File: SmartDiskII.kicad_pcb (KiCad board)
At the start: 2 copper layers, 100 x 77.5 mm, 32 parts, among them J1 DRIVE 2, J2 DRIVE 1, J3 Apple II Expansion Slot, U1 74LS174, U10 74LS245, U11 74LS323, U12 74LS00, U13 74LS20, U2 NE556, U3 74LS05, U4 74LS132, U5 74LS259/9334, U6 74LS21, U7 2758/16/32 P6, U8 74LS30, U9 2732

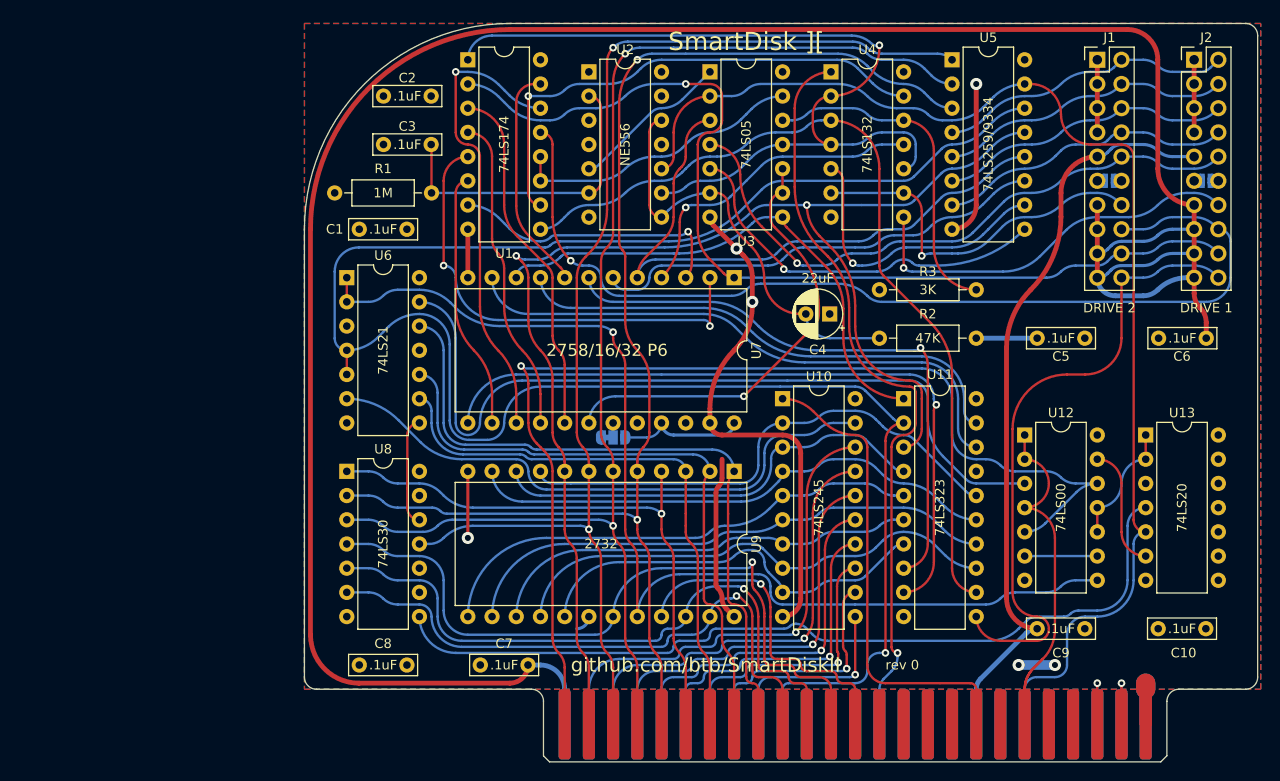
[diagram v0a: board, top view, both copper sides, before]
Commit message: new revision
only one drive connector, configurable with jumpers
optionally use 2764 EPROM
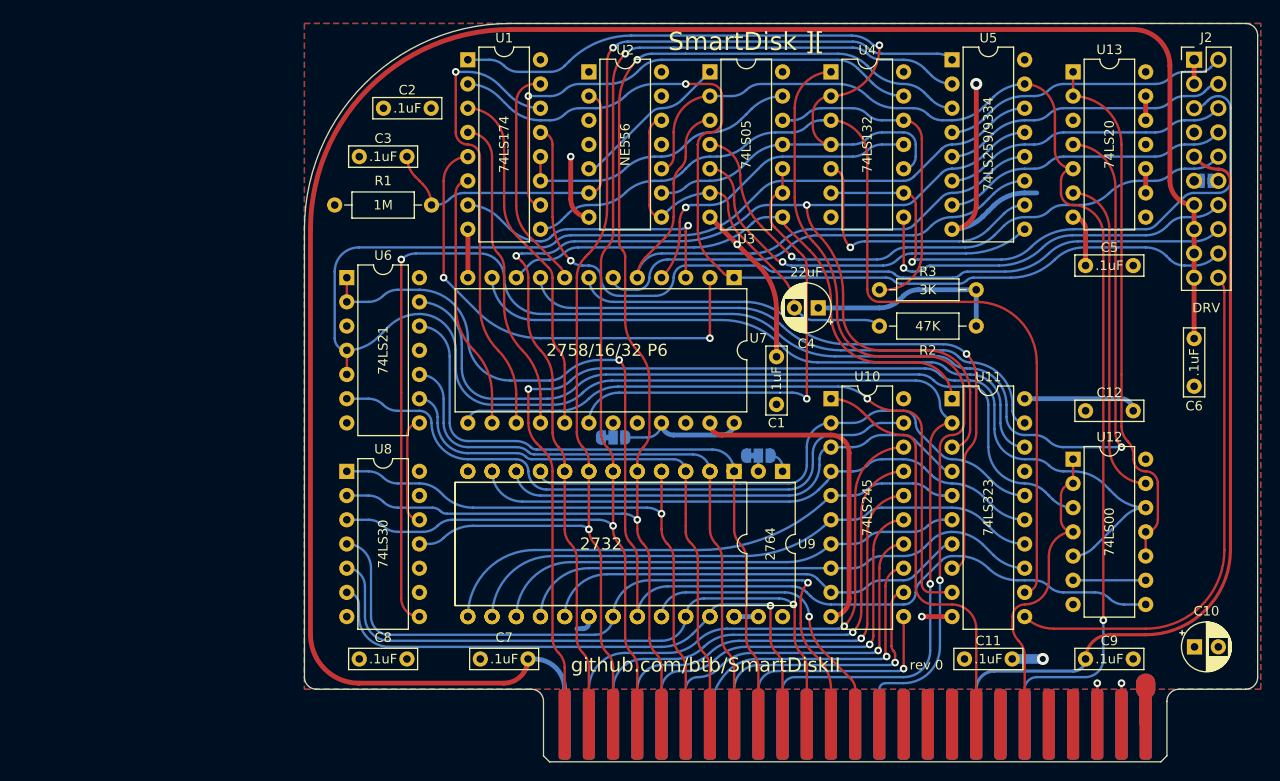
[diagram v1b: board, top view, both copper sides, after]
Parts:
- removed the J1 at (194.3, 67.3)
- removed JP2: 5V on Disk 2 Pin 12, Jumper:SolderJumper-2_P1.3mm_Open_RoundedPad1.0x1.5mm
- added ALTU9: 2764, Package_DIP:DIP-28_W15.24mm, F.Cu at (161.3, 110.5)
- added C11: .1uF, Capacitor_THT:C_Rect_L7.0mm_W2.0mm_P5.00mm, F.Cu at (185.4, 130.2)
- added C12: .1uF, Capacitor_THT:C_Rect_L7.0mm_W2.0mm_P5.00mm, F.Cu at (198.1, 104.1)
- added JP4: A12H/L, Jumper:SolderJumper-3_P1.3mm_Bridged12_RoundedPad1.0x1.5mm_NumberLabels, B.Cu at (158.8, 108.8)
- C10: value .1uF -> 22uF; footprint Capacitor_THT:C_Rect_L7.0mm_W2.0mm_P5.00mm -> Capacitor_THT:CP_Radial_D5.0mm_P2.50mm
- J2: value DRIVE 1 -> DRV
- moved C1 47.5 mm to (160.7, 103.5), turned to 90 degrees
- moved U13 38.9 mm to (191.8, 68.6)
- moved C5 12.6 mm to (198.1, 88.9), turned to 180 degrees
- moved R3 10.2 mm to (181.6, 91.4), turned to 180 degrees
- moved C9 5.99 mm to (193.1, 130.2)
- moved U12 5.68 mm to (191.8, 109.2)
- moved U10 5.08 mm to (166.4, 102.9)
- moved U11 5.08 mm to (179.1, 102.9)
- moved C10 4.26 mm to (204.5, 128.9)
- moved C3 2.84 mm to (121.9, 77.5)
- moved C4 1.36 mm to (165.0, 93.3)
- moved C6 1.27 mm to (204.5, 96.6), turned to -90 degrees
- moved C2 1.27 mm to (124.4, 72.4)
- moved R1 1.27 mm to (114.3, 82.5)
- moved R2 1.27 mm to (171.4, 95.2)
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- renumbered J3 to J1
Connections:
- net /SEL1 renamed /SEL
- J2 pad 5: GND -> /~{ENBL 2}
- J2 pad 7: GND -> unconnected-(J2-Pin_7-Pad7)
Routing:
- net /~{HISTROBE}: track 89.6 -> 157.9 mm, vias 0 -> 2
- net /ENCOMMON: track 12.9 -> 55.8 mm
- net +12V: track 252.2 -> 211.9 mm
- net /~{ENBL 2}: track 38.6 -> 64.5 mm
- net /CLRCOMMON: track 12.9 -> 34.5 mm
- net /RD DATA: track 104.4 -> 87.7 mm
- net +5V: track 45.4 -> 58.9 mm, vias 2 -> 1
- net /W PROT: track 66.3 -> 54.4 mm
- net Net-(U1-Cp): track 89.9 -> 100.0 mm
- net GND: track 103.9 -> 113.9 mm
- net /Q3: track 78.0 -> 86.7 mm
- net /~{ENROM}: track 115.7 -> 123.7 mm
- net /~{IOSTROBE}: track 39.5 -> 32.9 mm
- net /~{ENBUF}: track 60.9 -> 67.1 mm
- net /R/W: track 50.0 -> 44.1 mm
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
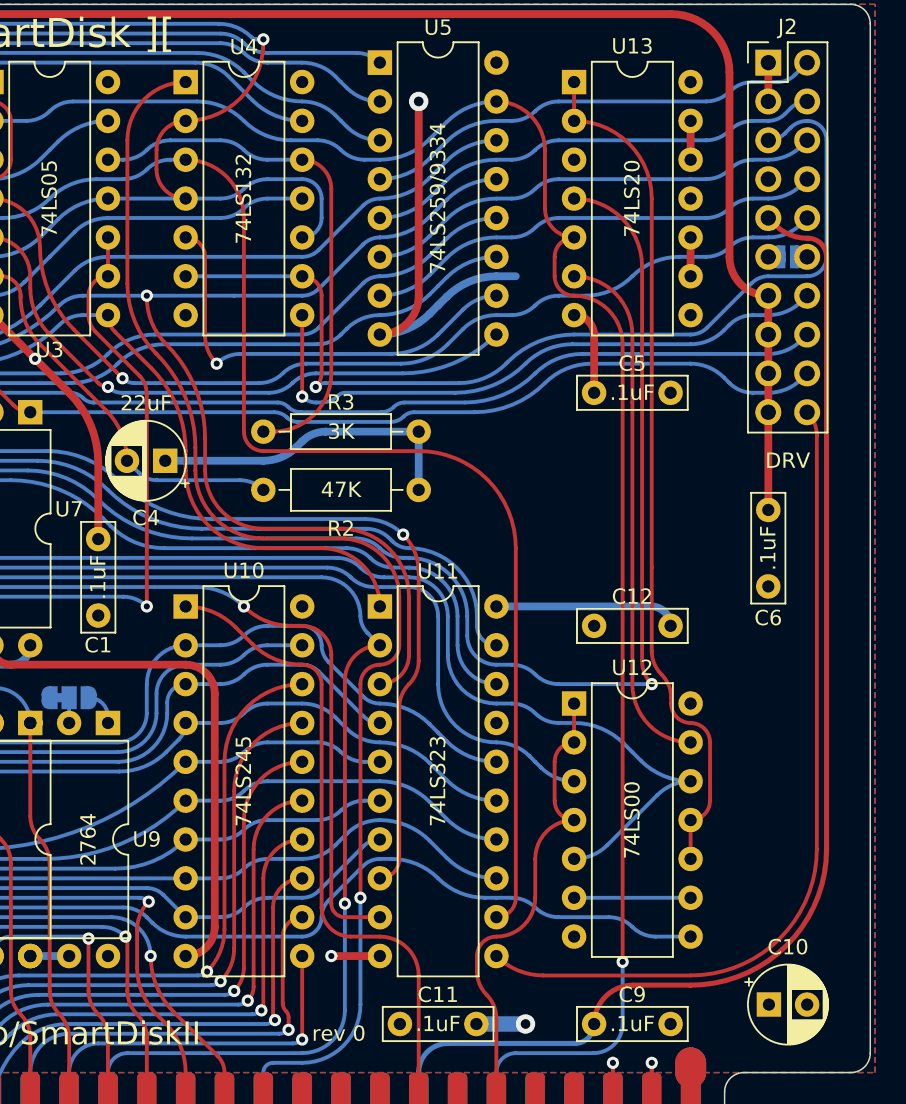
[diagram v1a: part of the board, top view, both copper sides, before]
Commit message: use liron pinout with jumpers for EN2
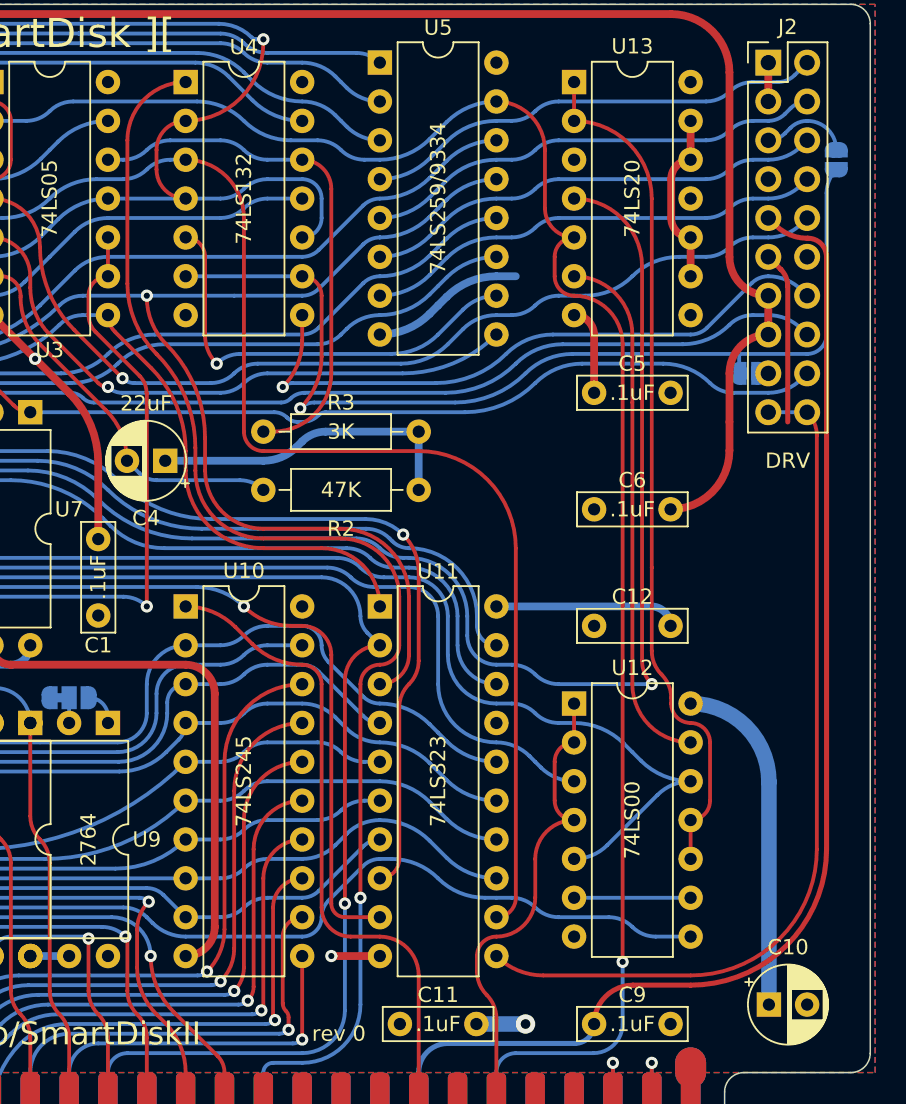
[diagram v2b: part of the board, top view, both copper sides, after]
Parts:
- added JP2: ~, Jumper:SolderJumper-2_P1.3mm_Open_RoundedPad1.0x1.5mm, B.Cu at (208.9, 73.7)
- JP1: value 5V on Disk 1 Pin 12 -> ~
- moved JP1 8.03 mm to (203.2, 87.6)
- moved C6 6.39 mm to (198.1, 96.5), turned to 180 degrees
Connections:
- J2 pad 17: +12V -> Net-(J2-Pin_17)
- J2 pad 19: +12V -> /W PROT
- J2 pad 5: /~{ENBL 2} -> Net-(J2-Pin_5)
- JP1 pad 1: +5V -> /~{ENBL 2}
- JP1 pad 2: /SEL -> Net-(J2-Pin_17)
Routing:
- net +5V: track 58.9 -> 92.6 mm
- net GND: track 113.9 -> 103.7 mm, vias 4 -> 3
- net Net-(J2-Pin_5): track 0.00 -> 5.83 mm
- net +12V: track 211.9 -> 215.3 mm
- net /W PROT: track 54.4 -> 56.9 mm
- net /~{ENBL 1}: track 40.3 -> 42.0 mm
- net /~{ENBL 2}: track 64.5 -> 65.5 mm

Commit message: update kicad files
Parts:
- added JP10: SolderJumper_2_Bridged, Jumper:SolderJumper-2_P1.3mm_Bridged_RoundedPad1.0x1.5mm, B.Cu at (112.4, 109.2)
- added JP11: SolderJumper_2_Bridged, Jumper:SolderJumper-2_P1.3mm_Bridged_RoundedPad1.0x1.5mm, B.Cu at (112.4, 101.6)
- added JP5: A13H/L, Connector_PinHeader_2.54mm:PinHeader_1x03_P2.54mm_Horizontal, F.Cu at (112.4, 118.1)
- added JP6: A14H/L, Connector_PinHeader_2.54mm:PinHeader_1x03_P2.54mm_Horizontal, F.Cu at (112.4, 110.5)
- added JP7: A15H/L, Connector_PinHeader_2.54mm:PinHeader_1x03_P2.54mm_Horizontal, F.Cu at (112.4, 102.9)
- added JP8: SolderJumper_2_Bridged, Jumper:SolderJumper-2_P1.3mm_Bridged_RoundedPad1.0x1.5mm, B.Cu at (112.4, 124.5)
- added JP9: SolderJumper_2_Bridged, Jumper:SolderJumper-2_P1.3mm_Bridged_RoundedPad1.0x1.5mm, B.Cu at (112.4, 116.8)
- added R4: 3K, Resistor_THT:R_Axial_DIN0207_L6.3mm_D2.5mm_P10.16mm_Horizontal, F.Cu at (198.1, 100.3)
- J2: footprint Connector_PinHeader_2.54mm:PinHeader_2x10_P2.54mm_Vertical -> MyConnector:PinHeader_2x10_P2.54mm_Vertical_Shrouded
- JP4: footprint Jumper:SolderJumper-3_P1.3mm_Bridged12_RoundedPad1.0x1.5mm_NumberLabels -> Connector_PinHeader_2.54mm:PinHeader_1x03_P2.54mm_Horizontal; moved to F.Cu
- moved JP4 49.3 mm to (112.4, 125.7), turned to 180 degrees
- moved JP3 3.43 mm to (143.5, 103.5), turned to 180 degrees
- moved C3 2.54 mm to (124.4, 77.5)
- moved J2 1.42 mm to (205.1, 68.6)
- moved JP2 0.90 mm to (209.6, 73.0)
- moved JP1 0.64 mm to (203.2, 88.3), turned to -90 degrees
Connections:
- net Net-(ALTU9-A12) renamed /FWA12
- ALTU9 pad 1: +5V -> /FWA15
- ALTU9 pad 26: +5V -> /FWA13
- ALTU9 pad 27: +5V -> /FWA14
- JP4 pad 1: GND -> +5V
- JP4 pad 3: +5V -> GND
- U9 pad 24: +5V -> /FWA13
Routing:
- net GND: track 103.7 -> 173.7 mm
- net /FWA15: track 0.00 -> 63.2 mm
- net /FWA12: track 1.65 -> 60.2 mm, vias 0 -> 1
- net /FWA14: track 0.00 -> 58.2 mm, vias 0 -> 1
- net /FWA13: track 0.00 -> 52.8 mm, vias 0 -> 1
- net Net-(U7-~{CE}): track 50.9 -> 78.2 mm, vias 1 -> 2
- net +5V: track 92.6 -> 114.6 mm
- net /~{IOSEL}: track 118.3 -> 126.3 mm
- net /IOSTROBE: track 84.4 -> 77.8 mm
- net /A4: track 61.4 -> 64.4 mm
- net Net-(J2-Pin_17): track 0.00 -> 1.91 mm
- net Net-(U11-SR): track 70.5 -> 72.3 mm
- net /R4: track 61.7 -> 59.9 mm
- net /R3: track 56.6 -> 54.8 mm
- net /R5: track 49.9 -> 48.3 mm
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
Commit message: rev2
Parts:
- removed JP10, JP11, JP8, JP9: SolderJumper_2_Bridged, Jumper:SolderJumper-2_P1.3mm_Bridged_RoundedPad1.0x1.5mm
- removed the JP4 at (112.4, 125.7)
- added C13: 100n, Capacitor_THT:C_Disc_D4.3mm_W1.9mm_P5.00mm, F.Cu at (193.0, 130.2)
- added C14: 100n, Capacitor_THT:C_Disc_D4.3mm_W1.9mm_P5.00mm, F.Cu at (205.7, 125.7)
- added JP3: ~, Jumper:SolderJumper-2_P1.3mm_Open_RoundedPad1.0x1.5mm, B.Cu at (206.4, 91.4)
- added R5: 10K, Resistor_THT:R_Axial_DIN0207_L6.3mm_D2.5mm_P10.16mm_Horizontal, F.Cu at (114.9, 90.2)
- added R6: 10K, Resistor_THT:R_Axial_DIN0207_L6.3mm_D2.5mm_P10.16mm_Horizontal, F.Cu at (114.9, 102.9)
- added R7: 10K, Resistor_THT:R_Axial_DIN0207_L6.3mm_D2.5mm_P10.16mm_Horizontal, F.Cu at (118.7, 102.9)
- added R8: 10K, Resistor_THT:R_Axial_DIN0207_L6.3mm_D2.5mm_P10.16mm_Horizontal, F.Cu at (118.7, 90.2)
- added SJP10: ~, Jumper:SolderJumper-2_P1.3mm_Bridged_RoundedPad1.0x1.5mm, F.Cu at (117.5, 118.1)
- added SJP8: ~, Jumper:SolderJumper-2_P1.3mm_Bridged_RoundedPad1.0x1.5mm, F.Cu at (117.5, 123.2)
- added SJP9: ~, Jumper:SolderJumper-2_P1.3mm_Bridged_RoundedPad1.0x1.5mm, F.Cu at (117.5, 120.7)
- ALTU10: renamed from ALTU9; value 2764 -> '64-'512
- C1: renamed from C4; value 22uF -> 22u
- C10: renamed from C2; value .1uF -> 100n; footprint Capacitor_THT:C_Rect_L7.0mm_W2.0mm_P5.00mm -> Capacitor_THT:C_Disc_D4.3mm_W1.9mm_P5.00mm
- C11, C12, C3, C5, C6, C7, C8, C9: value .1uF -> 100n; footprint Capacitor_THT:C_Rect_L7.0mm_W2.0mm_P5.00mm -> Capacitor_THT:C_Disc_D4.3mm_W1.9mm_P5.00mm
- C2: renamed from C10; value 22uF -> 22u
- C4: renamed from C1; value .1uF -> 100n; footprint Capacitor_THT:C_Rect_L7.0mm_W2.0mm_P5.00mm -> Capacitor_THT:C_Disc_D4.3mm_W1.9mm_P5.00mm
- JP5: value A13H/L -> ~; footprint Connector_PinHeader_2.54mm:PinHeader_1x03_P2.54mm_Horizontal -> Connector_PinHeader_2.54mm:PinHeader_1x02_P2.54mm_Vertical
- JP6: value A14H/L -> ~; footprint Connector_PinHeader_2.54mm:PinHeader_1x03_P2.54mm_Horizontal -> Connector_PinHeader_2.54mm:PinHeader_1x02_P2.54mm_Vertical
- JP7: value A15H/L -> ~; footprint Connector_PinHeader_2.54mm:PinHeader_1x03_P2.54mm_Horizontal -> Connector_PinHeader_2.54mm:PinHeader_1x02_P2.54mm_Vertical
- moved C8 91.9 mm to (198.7, 88.3), turned to 180 degrees
- moved C10 81.2 mm to (200.7, 100.3), turned to 0 degrees
- moved C12 73.8 mm to (129.5, 131.4)
- moved C11 70.4 mm to (115.0, 128.9), turned to 0 degrees
- moved C5 49.3 mm to (151.1, 73.7), turned to -90 degrees
- moved C4 46.9 mm to (117.5, 85.1), turned to 0 degrees
- moved C7 42.5 mm to (167.6, 103.5), turned to 90 degrees
- moved C9 38.7 mm to (193.7, 91.4)
- moved C6 31.0 mm to (177.2, 73.7), turned to -90 degrees
- moved JP7 16.5 mm to (118.8, 118.1), turned to -90 degrees
- moved JP6 12.0 mm to (118.8, 120.7), turned to -90 degrees
- moved U13 8.52 mm to (199.4, 105.4)
- moved JP5 8.14 mm to (118.8, 123.2), turned to -90 degrees
- moved ALTU10 7.62 mm to (168.9, 110.5)
- moved JP4 7.62 mm to (151.1, 103.5), turned to 0 degrees
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- renumbered JP2 to JP1, JP1 to JP2, JP3 to JP4, U9 to U10, U10 to U11, U11 to U12, U12 to U13, U13 to U6, U6 to U7, U7 to U8, U8 to U9
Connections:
- ALTU10 pad 1: /FWA15 -> Net-(ALTU10-A14)
- ALTU10 pad 2: /FWA12 -> GND
- ALTU10 pad 21: /A10 -> /FWA10
- ALTU10 pad 24: /A9 -> /FWA9
- ALTU10 pad 25: /A8 -> /FWA8
- ALTU10 pad 26: /FWA13 -> +5V
- ALTU10 pad 27: /FWA14 -> +5V
- C12 pad 1: +5V -> +12V
- C6 pad 1: +12V -> +5V
- C7 pad 1: +12V -> +5V
- C8 pad 1: +5V -> +12V
- C9 pad 1: -12V -> GND
- C9 pad 2: GND -> +5V
- J2 pad 19: /W PROT -> Net-(J2-Pin_19)
- JP5 pad 1: +5V -> /A8
- JP5 pad 2: /FWA13 -> /FWA8
- JP6 pad 1: +5V -> /A9
- JP6 pad 2: /FWA14 -> /FWA9
- JP7 pad 1: +5V -> /A10
- JP7 pad 2: /FWA15 -> /FWA10
- U10 pad 19: /A10 -> /FWA10
- U10 pad 22: /A9 -> /FWA9
- U10 pad 23: /A8 -> /FWA8
- U10 pad 24: /FWA13 -> +5V
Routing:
- net /FWA8: track 0.00 -> 75.4 mm
- net /FWA15: track 63.2 -> 0.00 mm
- net Net-(ALTU10-A14): track 0.00 -> 61.7 mm, vias 0 -> 1
- net +5V: track 114.6 -> 54.0 mm, vias 1 -> 0
- net /FWA12: track 60.2 -> 0.00 mm, vias 1 -> 0
- net /FWA14: track 58.2 -> 0.00 mm, vias 1 -> 0
- net /FWA9: track 0.00 -> 56.3 mm
- net /FWA13: track 52.8 -> 0.00 mm, vias 1 -> 0
- net /FWA10: track 0.00 -> 47.3 mm
- net /~{IOSTROBE}: track 32.9 -> 47.2 mm, vias 0 -> 1
- net Net-(U1-~{Mr}): track 92.2 -> 104.5 mm
- net /W PROT: track 56.6 -> 46.3 mm
- net Net-(U1-Q1): track 50.2 -> 58.9 mm
- net /Q3: track 86.7 -> 94.8 mm
- net Net-(U1-Q5): track 24.1 -> 32.0 mm
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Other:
- board text added: "J5,J6,J7 Closed - SmartPort J5,J6,J7 Open - Disk ]["
- board text added: "JLCJLCJLCJLC"

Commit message: All slot auto-switching rom
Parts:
- removed ALTU10: '64-'512, Package_DIP:DIP-28_W15.24mm
- removed JP7: ~, Connector_PinHeader_2.54mm:PinHeader_1x02_P2.54mm_Vertical
- removed R5, R6, R7, R8: 10K, Resistor_THT:R_Axial_DIN0207_L6.3mm_D2.5mm_P10.16mm_Horizontal
- removed SJP10, SJP8, SJP9: ~, Jumper:SolderJumper-2_P1.3mm_Bridged_RoundedPad1.0x1.5mm
- added JP8: ~, Connector_PinHeader_2.54mm:PinHeader_1x02_P2.54mm_Vertical, F.Cu at (116.2, 104.1)
- added R10: 10K, Resistor_THT:R_Axial_DIN0207_L6.3mm_D2.5mm_P10.16mm_Horizontal, F.Cu at (113.7, 100.3)
- added U14: 74LS174, Package_DIP:DIP-16_W7.62mm, F.Cu at (113.7, 109.2)
- JP5, JP6: footprint Connector_PinHeader_2.54mm:PinHeader_1x02_P2.54mm_Vertical -> Jumper:SolderJumper-3_P1.3mm_Bridged12_RoundedPad1.0x1.5mm_NumberLabels
- U10: value 2732 -> 27C256; footprint Package_DIP:DIP-24_W15.24mm -> Package_DIP:DIP-28_W15.24mm
- moved JP6 53.6 mm to (170.8, 108.0), turned to 0 degrees
- moved JP5 49.8 mm to (168.3, 128.3), turned to 0 degrees
- moved U10 6.98 mm to (170.8, 110.5)
- moved C7 3.18 mm to (170.8, 103.5)
- moved U7 2.54 mm to (125.7, 90.2)
- moved U9 2.54 mm to (125.7, 110.5)
- moved C11 2.54 mm to (115.0, 131.4)
- moved C12 2.54 mm to (132.0, 131.4)
- moved JP4 1.91 mm to (153.0, 103.5)
- moved U8 1.91 mm to (165.7, 90.2)
- moved C1 1.27 mm to (172.7, 92.1)
- moved U11 1.27 mm to (175.3, 102.9)
- moved C13 0.63 mm to (193.6, 130.2)
- moved U12 0.63 mm to (187.3, 102.9)
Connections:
- J1 pad 14: unconnected-(J1-Pin_14-Pad14) -> /A12
- J1 pad 15: unconnected-(J1-Pin_15-Pad15) -> /A13
- J1 pad 16: unconnected-(J1-Pin_16-Pad16) -> /A14
- JP5 pad 1: /A8 -> /LA14
- JP5 pad 2: /FWA8 -> Net-(JP5-C)
- JP6 pad 1: /A9 -> /LA14
- JP6 pad 2: /FWA9 -> Net-(JP6-C)
- U10 pad 1: /A7 -> Net-(JP6-C)
- U10 pad 10: /R1 -> /A0
- U10 pad 11: /R2 -> /R0
- U10 pad 12: GND -> /R1
- U10 pad 13: /R3 -> /R2
- U10 pad 14: /R4 -> GND
- U10 pad 15: /R5 -> /R3
- U10 pad 16: /R6 -> /R4
- U10 pad 17: /R7 -> /R5
- U10 pad 18: GND -> /R6
- U10 pad 19: /FWA10 -> /R7
- U10 pad 2: /A6 -> /LA12
- U10 pad 20: /~{ENROM} -> GND
- U10 pad 21: /A11 -> /A10
- U10 pad 22: /FWA9 -> /~{ENROM}
- U10 pad 23: /FWA8 -> /A11
- U10 pad 24: +5V -> /A9
- U10 pad 3: /A5 -> /A7
- U10 pad 4: /A4 -> /A6
- U10 pad 5: /A3 -> /A5
- U10 pad 6: /A2 -> /A4
- U10 pad 7: /A1 -> /A3
- U10 pad 8: /A0 -> /A2
- U10 pad 9: /R0 -> /A1
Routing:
- net /ENCOMMON: track 56.0 -> 186.7 mm, vias 0 -> 1
- net /FWA8: track 75.4 -> 0.00 mm
- net /LA14: track 0.00 -> 73.7 mm, vias 0 -> 1
- net /LA12: track 0.00 -> 63.8 mm, vias 0 -> 1
- net Net-(ALTU10-A14): track 61.7 -> 0.00 mm, vias 1 -> 0
- net /FWA9: track 56.3 -> 0.00 mm
- net /LA13: track 0.00 -> 54.9 mm
- net /FWA10: track 47.3 -> 0.00 mm
- net /A8: track 68.5 -> 58.5 mm, vias 1 -> 0
- net Net-(JP8-B): track 0.00 -> 8.89 mm
- net +5V: track 54.0 -> 62.8 mm
- net /A9: track 72.1 -> 64.4 mm
- net Net-(U1-Q1): track 58.9 -> 52.0 mm
- net /A10: track 76.6 -> 69.8 mm
- net GND: track 175.7 -> 169.4 mm
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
